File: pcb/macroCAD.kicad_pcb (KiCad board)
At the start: 2 copper layers, 81.2 x 62.8 mm, 27 parts, among them SW1 SW_Push, SW10 SW_Push, SW2 SW_Push, SW3 SW_Push, SW4 SW_Push, SW5 SW_Push, SW6 SW_Push, SW7 SW_Push, SW8 SW_Push, SW9 SW_Push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

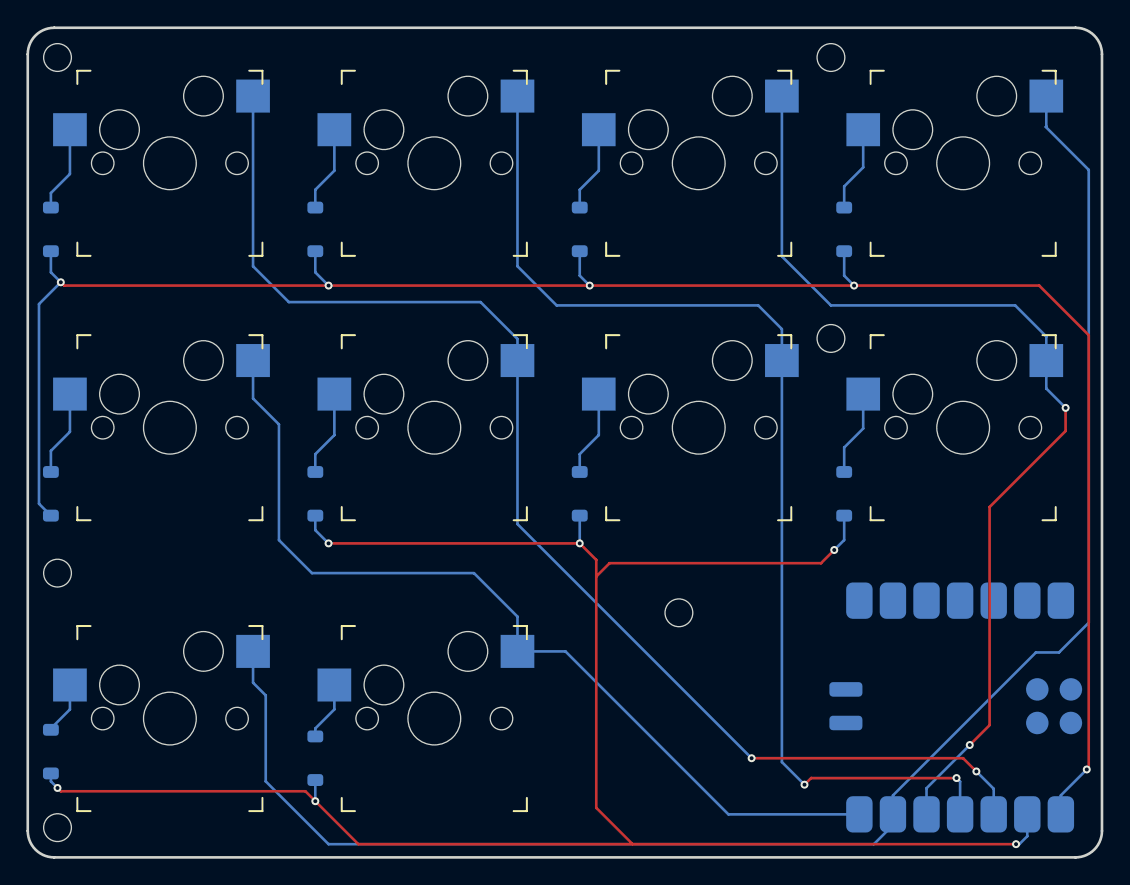
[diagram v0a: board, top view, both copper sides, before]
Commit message: Add GND plane to PCB
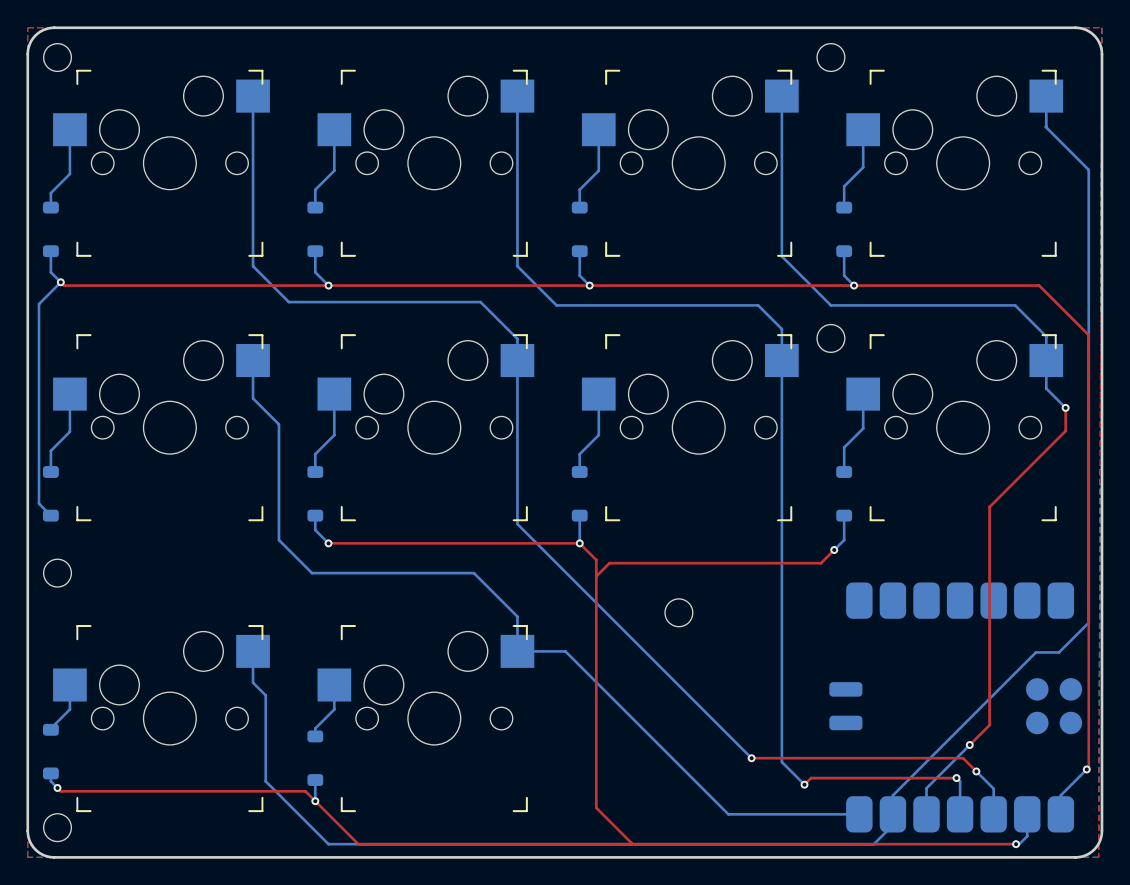
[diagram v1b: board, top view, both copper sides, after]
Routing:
- added copper zone on B.Cu, net GND
- added copper zone on F.Cu, net GND
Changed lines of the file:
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@@
 		(net 30)
+	)
+	(zone
+		(net 20)
+		(net_name "GND")
+		(layer "F.Cu")
+		(hatch edge 0.5)
+		(priority 1)
+		(connect_pads
+			(clearance 0.5)
+		)
+		(min_thickness 0.25)
+		(filled_areas_thickness no)
+		(fill yes
+			(thermal_gap 0.5)
+			(thermal_bridge_width 0.5)
+		)
+		(polygon
+			(pts
+				(xy 69.25 19.75) (xy 150.5 19.75) (xy 150.25 82.5) (xy 69.25 82.5)
+			)
+		)
+	)
+	(zone
+		(net 20)
+		(net_name "GND")
+		(layer "B.Cu")
+		(hatch edge 0.5)
+		(connect_pads
+			(clearance 0.5)
+		)
+		(min_thickness 0.25)
+		(filled_areas_thickness no)
+		(fill yes
+			(thermal_gap 0.5)
+			(thermal_bridge_width 0.5)
+		)
+		(polygon
+			(pts
+				(xy 69.25 19.75) (xy 150.5 19.75) (xy 150.25 82.5) (xy 69.25 82.5)
+			)
+		)
 	)
 	(embedded_fonts no)
